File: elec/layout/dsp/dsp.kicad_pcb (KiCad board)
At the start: 2 copper layers, 11 parts

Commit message: Use Nets
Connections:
- net R_DVDD renamed DVDD[1]

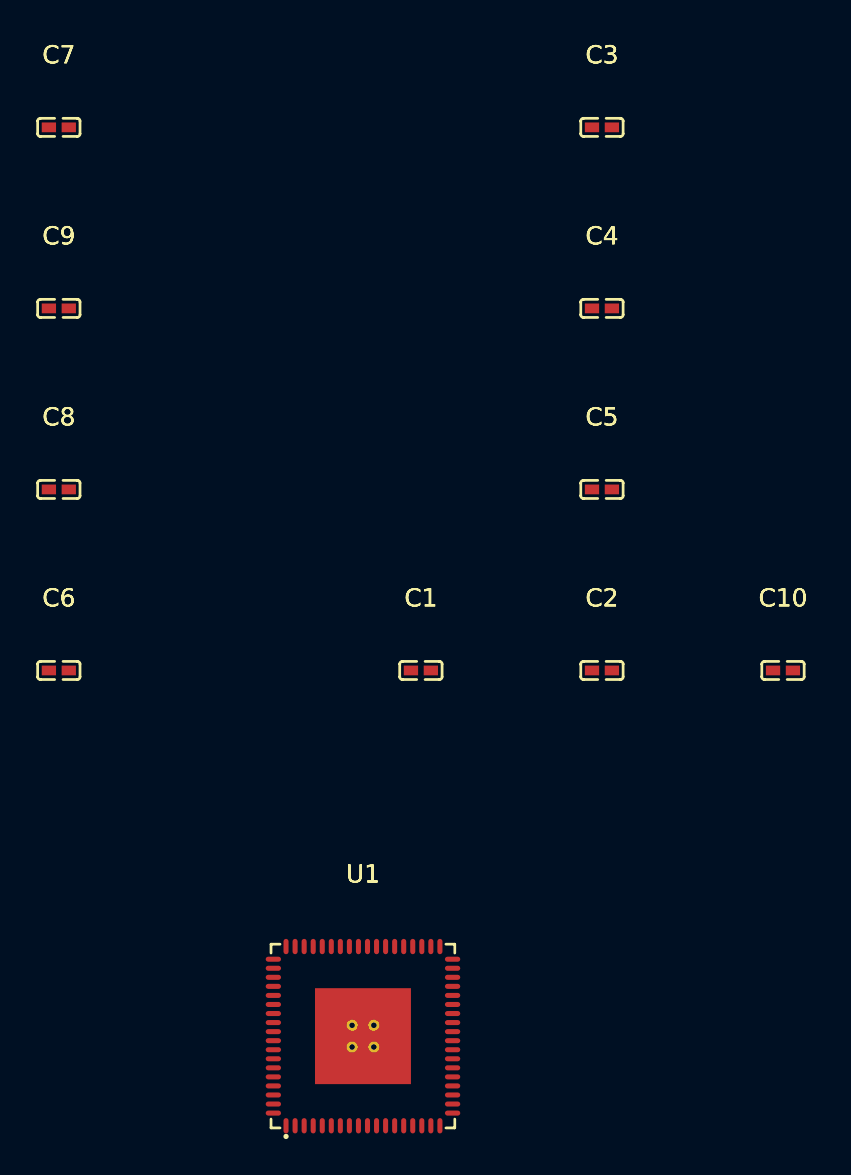
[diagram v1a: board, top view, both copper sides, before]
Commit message: upgrade to newest ato
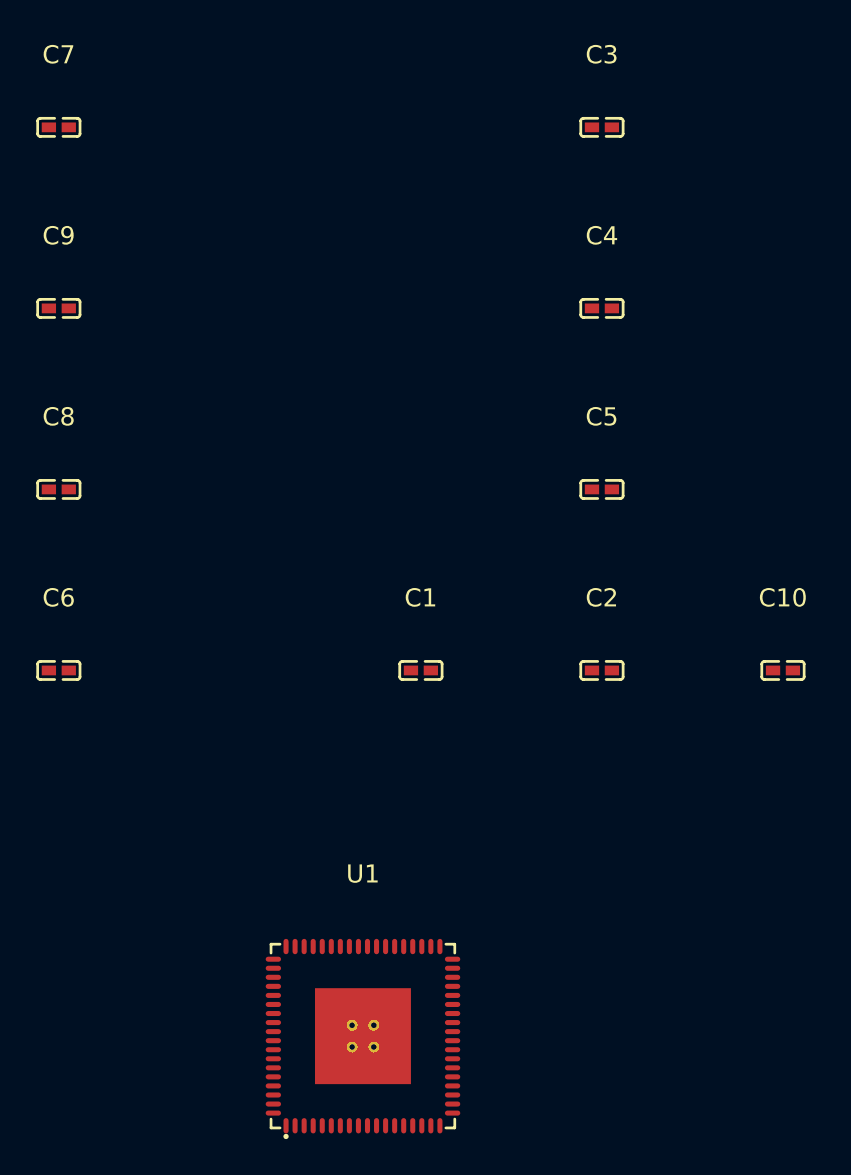
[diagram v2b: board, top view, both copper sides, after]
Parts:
- C1, C10, C2, C3, C4, C5, C6, C7, C8, C9: footprint atopile:C0402-b3ef17 -> Samsung_Electro_Mechanics_CL05B104KO5NNNC:C0402
- U1: footprint atopile:LFCSP-72_L10.0-W10.0-P0.50-LS10.2-BL-EP5.3-8f2bc3 -> Analog_Devices_ADAU1452WBCPZ:LFCSP-72_L10.0-W10.0-P0.50-LS10.2-BL-EP5.3
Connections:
- net DVDD[1] renamed N_DVDD
- U1 pad : (no net) -> net
